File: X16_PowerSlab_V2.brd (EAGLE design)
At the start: 152.4 x 76.2 mm, 43 parts, among them J4 796636-6

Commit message: fixed a resistor value
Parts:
- R1: value (none) -> 1k
- R2: value (none) -> 3.32k
- R4: value (none) -> 1M
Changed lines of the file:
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@@
 <drawing>
 <settings>
-<setting alwaysvectorfont="yes"/>
+<setting alwaysvectorfont="no"/>
 <setting verticaltext="up"/>
 </settings>
@@
 <attribute name="VALUE" x="34.2" y="14.628" size="1.27" layer="27"/>
 </element>
-<element name="R1" library="SparkFun-Resistors" library_urn="urn:adsk.eagle:library:532" package="0603" package3d_urn="urn:adsk.eagle:package:41389018/1" value=" " x="127.7112" y="38.7604" smashed="yes" rot="MR270">
+<element name="R1" library="SparkFun-Resistors" library_urn="urn:adsk.eagle:library:532" package="0603" package3d_urn="urn:adsk.eagle:package:41389018/1" value="1k" x="127.7112" y="38.7604" smashed="yes" rot="MR270">
 <attribute name="NAME" x="126.9492" y="38.7604" size="0.6096" layer="26" font="vector" ratio="20" rot="MR270" align="bottom-center"/>
 <attribute name="PROD_ID" value=" " x="259.7912" y="19.7104" size="1.778" layer="28" rot="MR270" display="off"/>
 <attribute name="VALUE" x="128.4732" y="38.7604" size="0.6096" layer="28" font="vector" ratio="20" rot="MR270" align="top-center"/>
 </element>
-<element name="R2" library="SparkFun-Resistors" library_urn="urn:adsk.eagle:library:532" package="0603" package3d_urn="urn:adsk.eagle:package:41389018/1" value=" " x="125.3998" y="38.6842" smashed="yes" rot="MR270">
+<element name="R2" library="SparkFun-Resistors" library_urn="urn:adsk.eagle:library:532" package="0603" package3d_urn="urn:adsk.eagle:package:41389018/1" value="3.32k" x="125.3998" y="38.6842" smashed="yes" rot="MR270">
 <attribute name="NAME" x="124.6378" y="38.6842" size="0.6096" layer="26" font="vector" ratio="20" rot="MR270" align="bottom-center"/>
 <attribute name="PROD_ID" value=" " x="257.4798" y="15.8242" size="1.778" layer="28" rot="MR270" display="off"/>
@@
 <attribute name="VALUE" x="129.3622" y="38.8112" size="0.6096" layer="28" font="vector" ratio="20" rot="MR90" align="top-center"/>
 </element>
-<element name="R4" library="SparkFun-Resistors" library_urn="urn:adsk.eagle:library:532" package="0603" package3d_urn="urn:adsk.eagle:package:41389018/1" value=" " x="34.6456" y="25.2222" smashed="yes" rot="R90">
+<element name="R4" library="SparkFun-Resistors" library_urn="urn:adsk.eagle:library:532" package="0603" package3d_urn="urn:adsk.eagle:package:41389018/1" value="1M" x="34.6456" y="25.2222" smashed="yes" rot="R90">
 <attribute name="NAME" x="33.8836" y="25.2222" size="0.6096" layer="25" font="vector" ratio="20" rot="R90" align="bottom-center"/>
 <attribute name="PROD_ID" value=" " x="166.7256" y="55.7022" size="1.778" layer="27" rot="R90" display="off"/>

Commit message: Minh Update
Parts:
- removed 12V_TP: TESTPOINT_5.04MM, X16-ExtraComponents:TESTPOINT_5.04MM
- removed 48V_TP: 48V, X16-ExtraComponents:TESTPOINT_5.04MM
- removed D2, D6: 12V, SparkFun-LED:LED-0805
- removed D3, D7: 5.2V, SparkFun-LED:LED-0805
- removed R5, R6: (no value), SparkFun-Resistors:0603
- added 12V: TESTPOINT_5.04MM, X16-ExtraComponents:TESTPOINT_5.04MM
- added 12V_LED: 12V, SparkFun-LED:LED-0805
- added 48V: 48V, X16-ExtraComponents:TESTPOINT_5.04MM
- added 5.2V_LED: 5.2V, SparkFun-LED:LED-0805
- C2: value 0.01uF -> 0.1uF
- CIN2: value 0.47uF -> 0.1uF
- moved BACK_EMF 25.9 mm to (98.0, 39.7), turned to 90 degrees
- moved R10 16.3 mm to (142.6, 9.91), flipped to the top, turned to 359.6 degrees
- moved R9 14.4 mm to (87.1, 36.9), turned to 90 degrees
- moved D5 3.79 mm to (14.3, 59.4)
- moved R8 3.79 mm to (10.5, 59.5)
- renumbered 48V_GND_TP to 48V_GND, 5.2V_TP to 5.2V, GND_TP to GND
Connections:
- removed net N$3: D2.A, R5.2
- removed net N$5: D3.A, R6.2
- net 12V: now also 12V.TP; no longer 12V_TP.TP, R5.1
- net 48V: now also 48V.TP; no longer 48V_TP.TP
- net 5.2V: no longer R6.1
- net GND: now also 12V_LED.C, 5.2V_LED.C; no longer D2.C, D3.C, D6.C, D7.C
- net N$10: now also 12V_LED.A; no longer D6.A
- net N$11: now also 5.2V_LED.A; no longer D7.A
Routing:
- net 12V: track 84.9 -> 105.2 mm, vias 5 -> 0
- net 48V: track 38.3 -> 43.5 mm
- net 5.2V: track 12.2 -> 16.4 mm, vias 1 -> 0
- net N$3: track 3.36 -> 0.00 mm
- net N$5: track 1.49 -> 0.00 mm
- net N$11: track 1.86 -> 2.42 mm
- net GND: track 51.8 -> 51.7 mm, vias 5 -> 4
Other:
- board text added: "48V_GND"
- board text added: "C:/Users/Minh/Downloads/crocs - Google Search.bmp"
- board text added: "CR2"
- board text added: "PMBUS_CTRL"
- board text added: "PMBUS_GND"
- board text added: "PMBUS_SA0"
- board text added: "PMBUS_SA1"
- board text added: "PMBUS_SALERT"
- board text added: "PMBUS_SCL"
- board text added: "PMBUS_SDA"
- board text removed: "GND_RAW"
- board text removed: "L1"

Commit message: Minh Update 2
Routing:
- net GND: vias 4 -> 28
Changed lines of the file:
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@@
 <setting verticaltext="up"/>
 </settings>
-<grid distance="1" unitdist="mil" unit="mil" style="lines" multiple="1" display="yes" altdistance="1" altunitdist="mil" altunit="mil"/>
+<grid distance="50" unitdist="mil" unit="mil" style="lines" multiple="1" display="yes" altdistance="1" altunitdist="mil" altunit="mil"/>
 <layers>
 <layer number="1" name="Top" color="4" fill="1" visible="yes" active="yes"/>
@@
 <wire x1="131.998" y1="35.3118" x2="131.998" y2="33.782" width="0.508" layer="16"/>
 <wire x1="130.1242" y1="37.1856" x2="131.998" y2="35.3118" width="0.508" layer="16"/>
+<via x="116.84" y="39.37" extent="1-16" drill="0.35"/>
+<via x="116.84" y="35.56" extent="1-16" drill="0.35"/>
+<via x="116.84" y="31.75" extent="1-16" drill="0.35"/>
+<via x="116.84" y="27.94" extent="1-16" drill="0.35"/>
+<via x="116.84" y="24.13" extent="1-16" drill="0.35"/>
+<via x="116.84" y="20.32" extent="1-16" drill="0.35"/>
+<via x="116.84" y="43.18" extent="1-16" drill="0.35"/>
+<via x="116.84" y="46.99" extent="1-16" drill="0.35"/>
+<via x="120.65" y="43.18" extent="1-16" drill="0.35"/>
+<via x="120.65" y="35.56" extent="1-16" drill="0.35"/>
+<via x="120.65" y="31.75" extent="1-16" drill="0.35"/>
+<via x="120.65" y="27.94" extent="1-16" drill="0.35"/>
+<via x="120.65" y="24.13" extent="1-16" drill="0.35"/>
+<via x="120.65" y="20.32" extent="1-16" drill="0.35"/>
+<via x="113.03" y="46.99" extent="1-16" drill="0.35"/>
+<via x="109.22" y="46.99" extent="1-16" drill="0.35"/>
+<via x="113.03" y="43.18" extent="1-16" drill="0.35"/>
+<via x="124.46" y="43.18" extent="1-16" drill="0.35"/>
+<via x="142.24" y="46.99" extent="1-16" drill="0.35"/>
+<via x="146.05" y="46.99" extent="1-16" drill="0.35"/>
+<via x="149.86" y="46.99" extent="1-16" drill="0.35"/>
+<via x="149.86" y="43.18" extent="1-16" drill="0.35"/>
+<via x="146.05" y="43.18" extent="1-16" drill="0.35"/>
+<via x="142.24" y="43.18" extent="1-16" drill="0.35"/>
 </signal>
 <signal name="N$1">

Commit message: Minh Update 3
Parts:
- added R3: 150k, SparkFun-Resistors:0603
- added R5: 220k, SparkFun-Resistors:0603
- R10: value 0.1 -> 250
- R8: value 0.1 -> 10k
- R9: value 0.1 -> 500
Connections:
- removed net PMBUS_GND: BACKPLANE_CONN.22, BMR480_POWERBRICK.PIN10
- net GND: now also BACKPLANE_CONN.22, BMR480_POWERBRICK.PIN10, R3.2, R5.2
- net PMBUS_SA0: now also R3.1; no longer BACKPLANE_CONN.17
- net PMBUS_SA1: now also R5.1; no longer BACKPLANE_CONN.18
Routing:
- net GND: track 51.7 -> 123.4 mm, vias 28 -> 26
- net PMBUS_GND: track 67.3 -> 0.00 mm
- net PMBUS_SA1: track 59.7 -> 53.7 mm
- net PMBUS_SA0: track 57.7 -> 52.0 mm
- net 12V: track 105.2 -> 104.0 mm

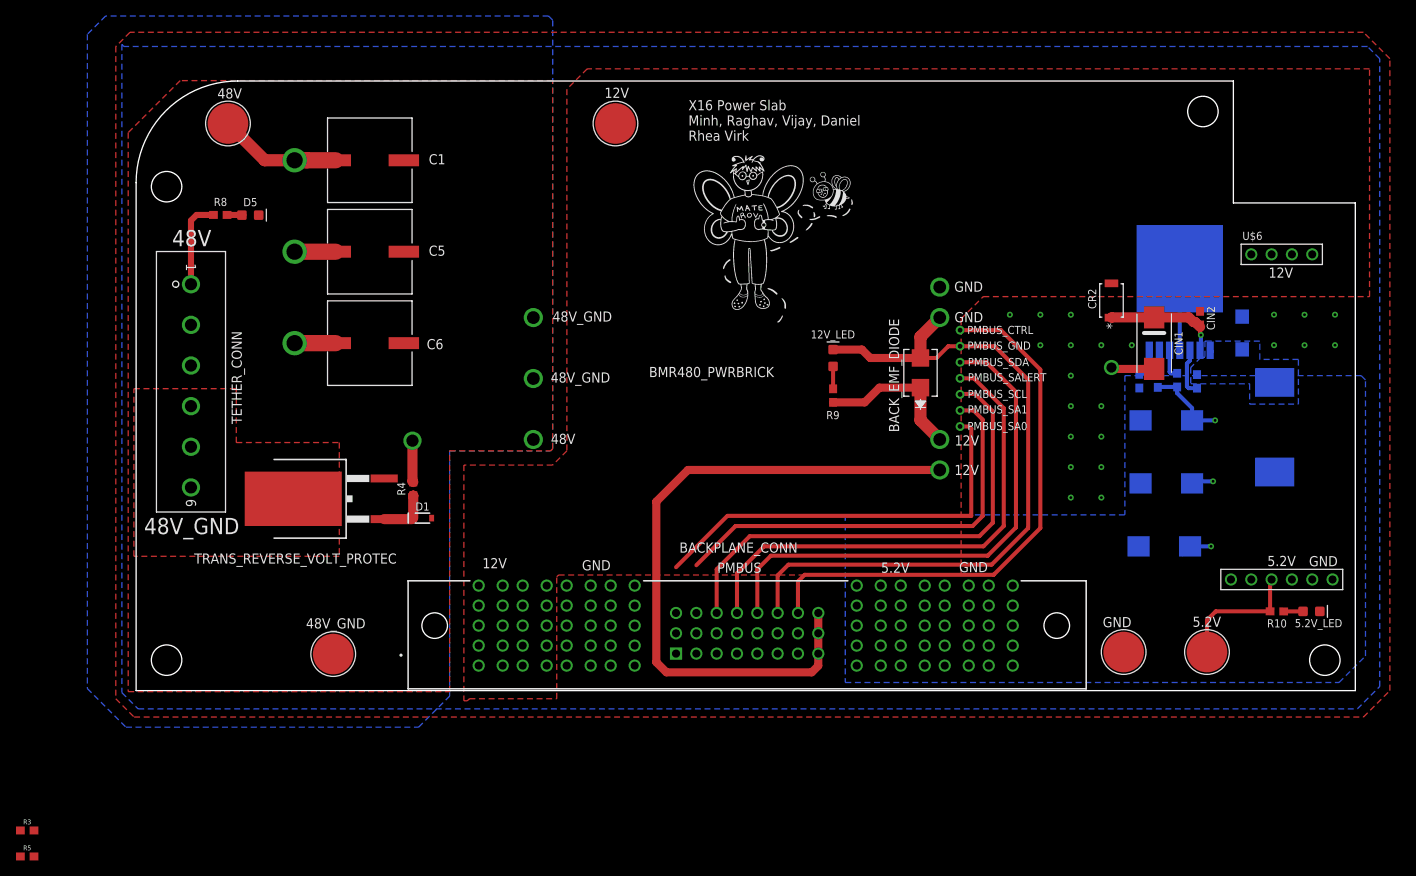
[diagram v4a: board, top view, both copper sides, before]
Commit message: Removed the traces, and placed the address resistors.
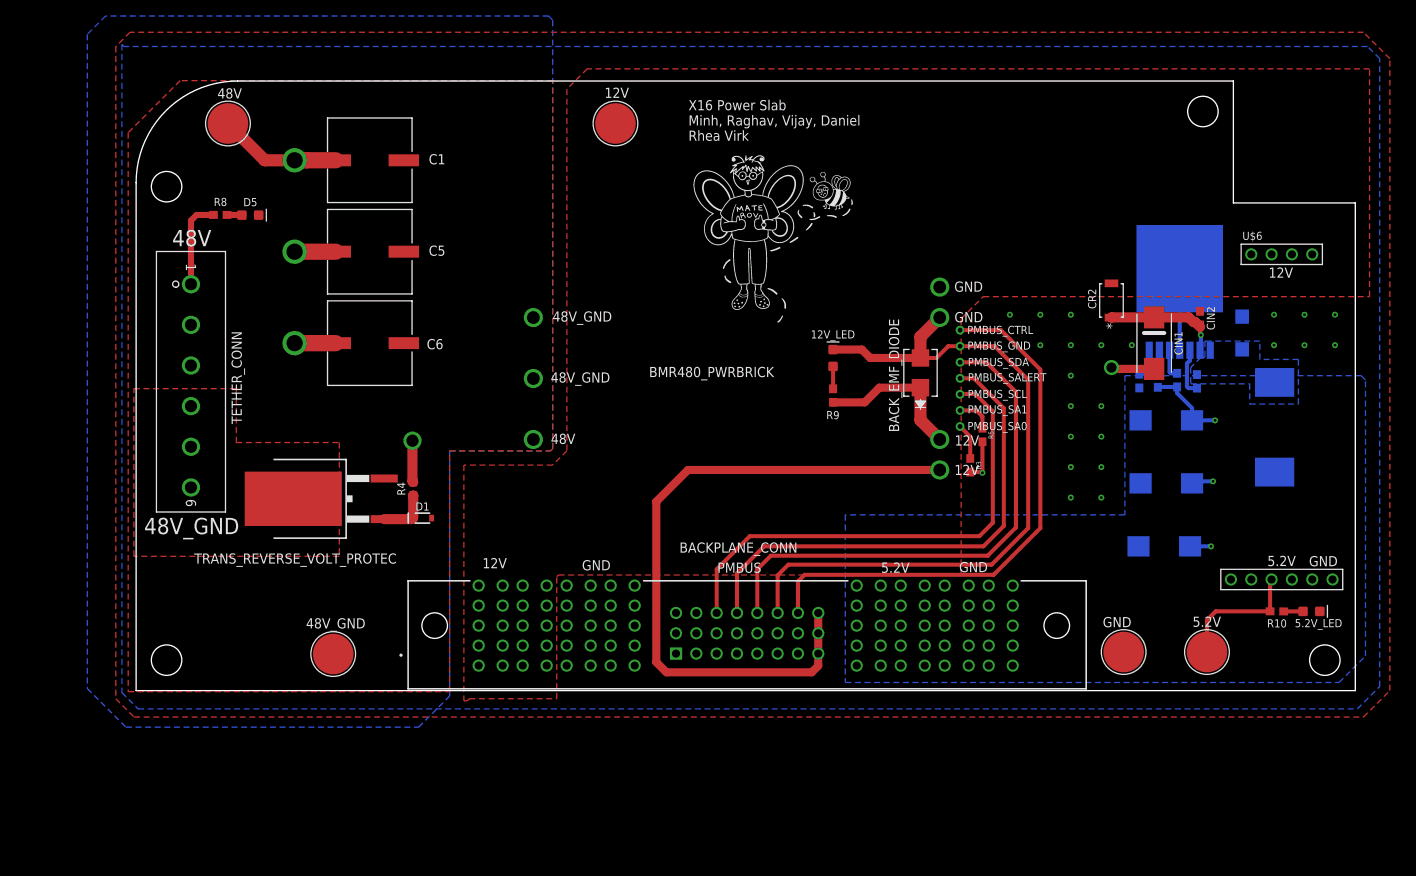
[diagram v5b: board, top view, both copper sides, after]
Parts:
- moved R5 130.5 mm to (105.8, 32.0), turned to 270 degrees
- moved R3 126.4 mm to (104.3, 28.2), turned to 270 degrees
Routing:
- net PMBUS_SA1: track 53.7 -> 4.57 mm
- net PMBUS_SA0: track 52.0 -> 4.53 mm
- net GND: track 123.4 -> 128.6 mm, vias 26 -> 27
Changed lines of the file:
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@@
 <attribute name="VALUE" x="122.174" y="3.429" size="0.0254" layer="27"/>
 </element>
-<element name="R3" library="SparkFun-Resistors" library_urn="urn:adsk.eagle:library:532" package="0603" package3d_urn="urn:adsk.eagle:package:41389018/1" value="150k" x="-13.6144" y="-17.4752" smashed="yes">
-<attribute name="NAME" x="-13.6144" y="-16.7132" size="0.6096" layer="25" font="vector" ratio="20" align="bottom-center"/>
-<attribute name="PROD_ID" value="RES-15715" x="-13.462" y="-17.4752" size="1.778" layer="27" display="off"/>
-<attribute name="VALUE" x="-13.6144" y="-18.2372" size="0.6096" layer="27" font="vector" ratio="20" align="top-center"/>
+<element name="R3" library="SparkFun-Resistors" library_urn="urn:adsk.eagle:library:532" package="0603" package3d_urn="urn:adsk.eagle:package:41389018/1" value="150k" x="104.267" y="28.1686" smashed="yes" rot="R270">
+<attribute name="NAME" x="105.029" y="28.1686" size="0.6096" layer="25" font="vector" ratio="20" rot="R270" align="bottom-center"/>
+<attribute name="PROD_ID" value="RES-15715" x="104.267" y="28.0162" size="1.778" layer="27" rot="R270" display="off"/>
+<attribute name="VALUE" x="103.505" y="28.1686" size="0.6096" layer="27" font="vector" ratio="20" rot="R270" align="top-center"/>
 </element>
-<element name="R5" library="SparkFun-Resistors" library_urn="urn:adsk.eagle:library:532" package="0603" package3d_urn="urn:adsk.eagle:package:41389018/1" value="220k" x="-13.6144" y="-20.7264" smashed="yes">
-<attribute name="NAME" x="-13.6144" y="-19.9644" size="0.6096" layer="25" font="vector" ratio="20" align="bottom-center"/>
-<attribute name="PROD_ID" value="RES-15715" x="-13.462" y="-20.7264" size="1.778" layer="27" display="off"/>
-<attribute name="VALUE" x="-13.6144" y="-21.4884" size="0.6096" layer="27" font="vector" ratio="20" align="top-center"/>
+<element name="R5" library="SparkFun-Resistors" library_urn="urn:adsk.eagle:library:532" package="0603" package3d_urn="urn:adsk.eagle:package:41389018/1" value="220k" x="105.791" y="31.9532" smashed="yes" rot="R270">
+<attribute name="NAME" x="106.553" y="31.9532" size="0.6096" layer="25" font="vector" ratio="20" rot="R270" align="bottom-center"/>
+<attribute name="PROD_ID" value="RES-15715" x="105.791" y="31.8008" size="1.778" layer="27" rot="R270" display="off"/>
+<attribute name="VALUE" x="105.029" y="31.9532" size="0.6096" layer="27" font="vector" ratio="20" rot="R270" align="top-center"/>
 </element>
 </elements>
@@
 <wire x1="107.3174" y1="43.0506" x2="111.506" y2="38.862" width="0.508" layer="1"/>
 <wire x1="102.993" y1="43.0506" x2="107.3174" y2="43.0506" width="0.508" layer="1"/>
-<wire x1="100.584" y1="46.501" x2="100.453" y2="46.632" width="0.508" layer="1"/>
 <wire x1="101.5214" y1="43.0506" x2="100.0506" y2="41.5798" width="0.508" layer="1"/>
 <wire x1="98.044" y1="41.5798" x2="100.0506" y2="41.5798" width="0.508" layer="1"/>
@@
 <contactref element="R3" pad="2"/>
 <contactref element="R5" pad="2"/>
-<wire x1="-12.7644" y1="-17.4752" x2="-12.7644" y2="-20.7264" width="0" layer="19" extent="1-1"/>
-<wire x1="53.82" y1="3.128" x2="-12.7644" y2="-17.4752" width="0" layer="19" extent="1-1"/>
+<wire x1="105.791" y1="31.1032" x2="105.791" y2="27.2288" width="0.508" layer="1"/>
+<via x="105.791" y="27.2288" extent="1-16" drill="0.35"/>
+<wire x1="104.267" y1="27.3186" x2="105.7012" y2="27.3186" width="0.508" layer="1"/>
+<wire x1="105.7012" y1="27.3186" x2="105.791" y2="27.2288" width="0.508" layer="1"/>
 </signal>
 <signal name="N$1">
@@
 <signal name="PMBUS_SA1">
 <contactref element="BMR480_POWERBRICK" pad="PIN14"/>
-<wire x1="70.03" y1="15.674" x2="74.93" y2="20.574" width="0.508" layer="1"/>
-<wire x1="105.8164" y1="21.82445" x2="105.8164" y2="33.8836" width="0.508" layer="1"/>
-<wire x1="104.56595" y1="20.574" x2="105.8164" y2="21.82445" width="0.508" layer="1"/>
-<wire x1="105.8164" y1="33.8836" x2="104.6758" y2="35.0242" width="0.508" layer="1"/>
-<wire x1="104.6758" y1="35.0242" x2="102.993" y2="35.0242" width="0.508" layer="1"/>
-<wire x1="74.93" y1="20.574" x2="104.56595" y2="20.574" width="0.508" layer="1"/>
 <contactref element="R5" pad="1"/>
-<wire x1="-14.4644" y1="-20.7264" x2="70.03" y2="15.674" width="0" layer="19" extent="1-1"/>
+<wire x1="102.993" y1="35.0242" x2="105.0314" y2="35.0242" width="0.508" layer="1"/>
+<wire x1="105.791" y1="34.2646" x2="105.791" y2="32.8032" width="0.508" layer="1"/>
+<wire x1="105.0314" y1="35.0242" x2="105.791" y2="34.2646" width="0.508" layer="1"/>
 </signal>
 <signal name="PMBUS_SA0">
 <contactref element="BMR480_POWERBRICK" pad="PIN15"/>
-<wire x1="104.394" y1="21.844" x2="104.394" y2="32.766" width="0.508" layer="1"/>
-<wire x1="67.49" y1="15.42" x2="73.914" y2="21.844" width="0.508" layer="1"/>
-<wire x1="73.914" y1="21.844" x2="104.394" y2="21.844" width="0.508" layer="1"/>
-<wire x1="104.394" y1="32.766" x2="104.1424" y2="33.0176" width="0.508" layer="1"/>
-<wire x1="102.993" y1="33.0176" x2="104.1424" y2="33.0176" width="0.508" layer="1"/>
 <contactref element="R3" pad="1"/>
-<wire x1="-14.4644" y1="-17.4752" x2="67.49" y2="15.42" width="0" layer="19" extent="1-1"/>
+<wire x1="102.993" y1="33.0176" x2="104.267" y2="31.7436" width="0.508" layer="1"/>
+<wire x1="104.267" y1="31.7436" x2="104.267" y2="29.0186" width="0.508" layer="1"/>
 </signal>
 <signal name="VIN">
